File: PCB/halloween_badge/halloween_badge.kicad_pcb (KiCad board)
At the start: 2 copper layers, 50 x 50 mm, 19 parts, among them U1 ATtiny48-A

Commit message: first finished PCB design
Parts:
- added D5: LED_Filled, LED_SMD:LED_0603_1608Metric_Pad1.05x0.95mm_HandSolder, F.Cu at (148.5, 109.5)
- added R6: R, Resistor_SMD:R_0402_1005Metric_Pad0.72x0.64mm_HandSolder, F.Cu at (148.5, 105.0)
- added SW1: SW_SPDT, Button_Switch_SMD:SW_SPDT_CK_JS102011SAQN, F.Cu at (134.0, 108.0)
- BT1: footprint Battery:BatteryHolder_Keystone_3002_1x2032 -> Connector_PinHeader_2.54mm:PinHeader_2x01_P2.54mm_Vertical_SMD
- C1, C2: footprint Capacitor_SMD:C_0805_2012Metric_Pad1.18x1.45mm_HandSolder -> Capacitor_SMD:C_0402_1005Metric_Pad0.74x0.62mm_HandSolder
- R1, R2, R3, R4, R5: footprint Resistor_SMD:R_0805_2012Metric_Pad1.20x1.40mm_HandSolder -> Resistor_SMD:R_0402_1005Metric_Pad0.72x0.64mm_HandSolder
- moved BT1 58.6 mm to (141.0, 117.0), turned to -45 degrees
- moved TP3 15.0 mm to (150.5, 85.0)
- moved TP6 14.5 mm to (143.0, 85.0)
- moved TP2 14.1 mm to (140.5, 85.0)
- moved TP4 14.0 mm to (148.0, 85.0)
- moved TP5 13.8 mm to (145.5, 85.0)
- moved R1 11.3 mm to (153.0, 96.5), turned to -90 degrees
- moved R4 5.39 mm to (147.0, 105.0), turned to -90 degrees
- moved R5 5.39 mm to (150.0, 105.0), turned to -90 degrees
- moved C1 2.00 mm to (141.0, 93.1)
- moved C2 1.52 mm to (153.0, 94.1)
- moved R2 1.12 mm to (145.5, 105.0), turned to -90 degrees
- moved R3 1.12 mm to (151.5, 105.0), turned to -90 degrees
- moved U1 0.93 mm to (147.0, 94.1), turned to 180 degrees
- moved TP1 0.50 mm to (152.0, 87.5)
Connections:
- U1 pad 24: unconnected-(U1-PC1-Pad24) -> /led_eye_left
- U1 pad 25: unconnected-(U1-PC2-Pad25) -> /led_mouth_left
- U1 pad 26: unconnected-(U1-PC3-Pad26) -> /led_nose
- U1 pad 27: unconnected-(U1-PC4-Pad27) -> /led_mouth_right
- U1 pad 28: unconnected-(U1-PC5-Pad28) -> /led_eye_right
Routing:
- net +BATT: track 0.00 -> 39.4 mm
- net /nRST: track 0.00 -> 20.4 mm
- net Net-(BT1-+): track 0.00 -> 8.97 mm
- net Net-(D4-A): track 0.00 -> 8.86 mm
- net Net-(D3-A): track 0.00 -> 8.86 mm
- net /led_eye_left: track 0.00 -> 8.67 mm
- net /led_eye_right: track 0.00 -> 8.11 mm
- net /led_mouth_right: track 0.00 -> 7.82 mm
- net /led_nose: track 0.00 -> 7.53 mm
- net /led_mouth_left: track 0.00 -> 7.24 mm
- net /SCK: track 0.00 -> 6.37 mm
- net /MOSI: track 0.00 -> 6.06 mm
- net /MISO: track 0.00 -> 5.36 mm
- net Net-(D5-A): track 0.00 -> 4.26 mm
- net GND: track 0.00 -> 3.91 mm
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- added copper zone on F.Cu, net GND
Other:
- board size 50 x 50 mm -> 40.2 x 43.8 mm

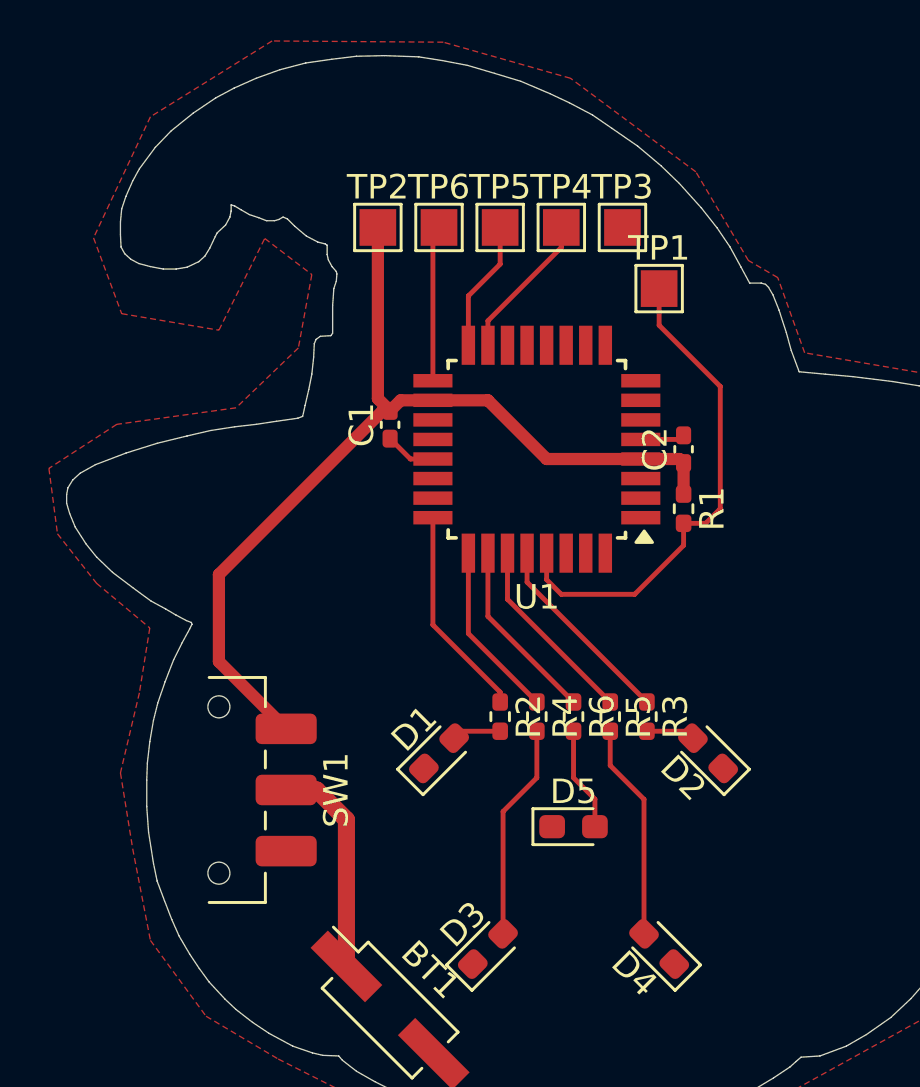
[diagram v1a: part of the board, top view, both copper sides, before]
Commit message: increased width of traces, added graphics
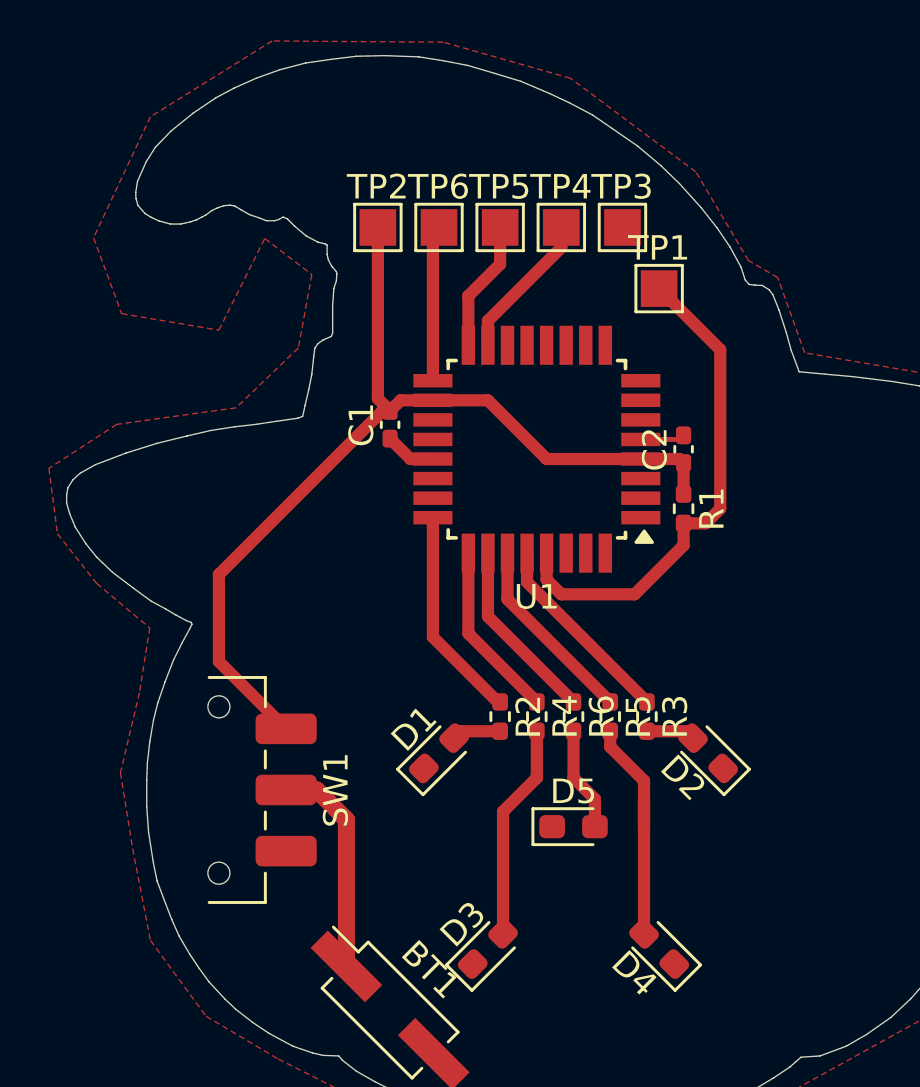
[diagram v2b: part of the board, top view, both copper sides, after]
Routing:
- net Net-(D4-A): track 8.86 -> 9.97 mm
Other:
- outline, holes or cut-outs redrawn
